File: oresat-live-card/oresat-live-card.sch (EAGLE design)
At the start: 277 parts, among them J1 ORESAT-DEBUG-CONNECTOR-CARD, J100 DM3BT-DSF-PEJS, J102 FTSH-105-XX-X-DV-K, J2 SM06B-SRSS-TB(LF)(SN), J4 TFM-120-01-L-D-RA, Q1 MMBT2907, Q2 PMV45EN, Q3 DMP2240UDM, Q4 PMV45EN, Q5 MOSFET-PCH-SOT23-6, Q6 MOSFET-PCH-SOT23-6, U1 RCLAMP0504FB, U10 TLVH431, U11 TCAN330, U12 MIC842LYC5, U13 MIC842LYC5, U14 MAX4211FETE, U15 TPS62112, U16 MAX7310ATE, U17 25AAXX, U18 RCLAMP0504FB, U2 TPS2051CDBVR, U3 THGBMJG7C2LBAU8, U4 SN74LVC1G07DCK, U7 OSD3358-512M-BSM, Y1 24MHz, Y2 ABS07-32.768KHZ-T

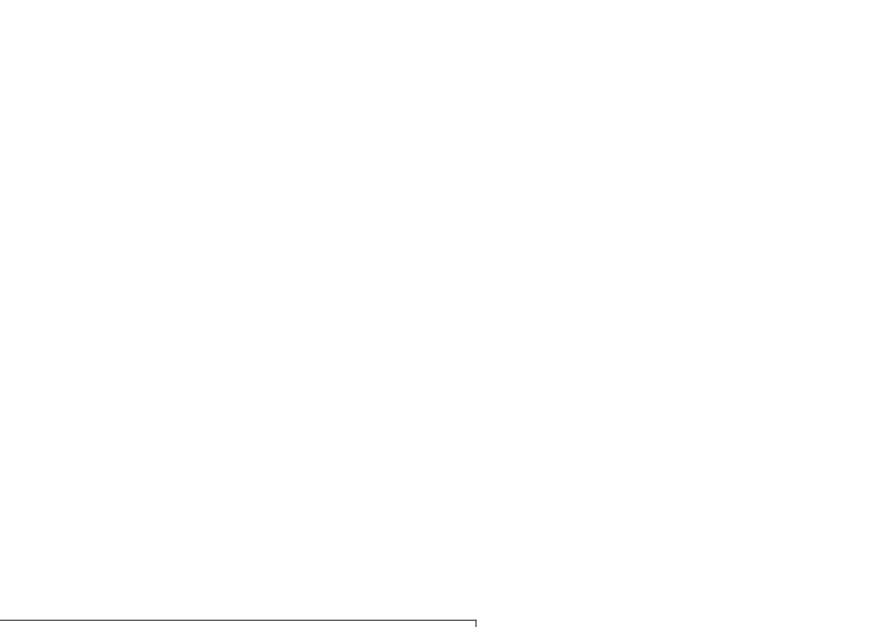
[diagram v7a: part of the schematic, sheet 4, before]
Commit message: routed usb host data for the wifi midule
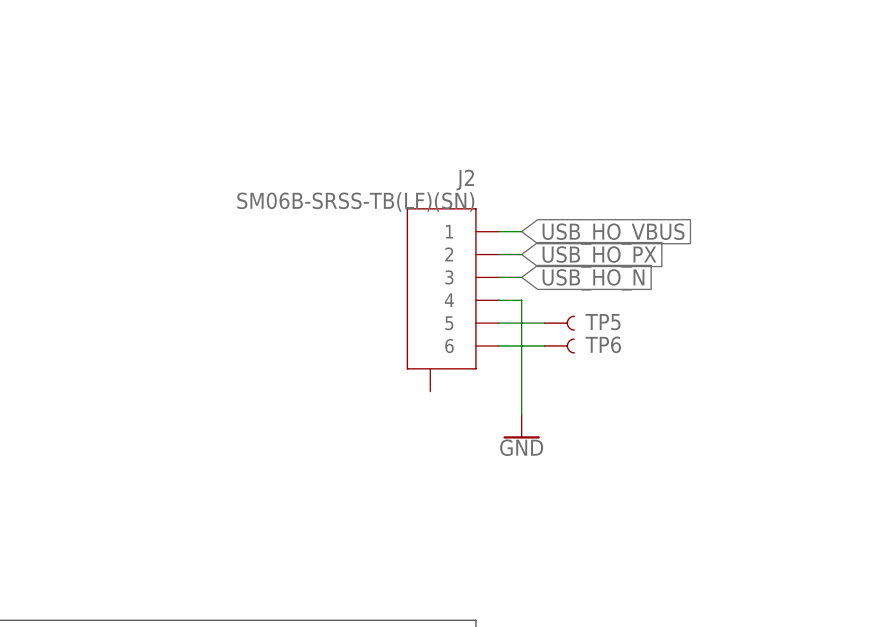
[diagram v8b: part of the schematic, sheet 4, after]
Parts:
- added TP5, TP6: TEST-POINT3X4, SparkFun-Connectors:TEST-POINT3X4
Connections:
- new net N$120: J2.5, TP5.1
- new net N$121: J2.6, TP6.1
- net GND: now also J2.4
- net USB_HO_N: now also J2.3
- net USB_HO_PX: now also J2.2
- net USB_HO_VBUS: now also J2.1
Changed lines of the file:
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@@
 <part name="PCBA1" library="PCBA-WF-NP9202-wifi-adapter" deviceset="WF-NP9202" device="WF"/>
 <part name="J2" library="J-JST-SM06B-SRSS-TB(LF)(SN)-1mm-smt-6pin" deviceset="SM06B-SRSS-TB(LF)(SN)" device=""/>
+<part name="GND33" library="SparkFun-PowerSymbols" deviceset="GND" device=""/>
+<part name="TP5" library="SparkFun-Connectors" deviceset="TEST-POINT" device="3X4" package3d_urn="urn:adsk.eagle:package:38287/1"/>
+<part name="TP6" library="SparkFun-Connectors" deviceset="TEST-POINT" device="3X4" package3d_urn="urn:adsk.eagle:package:38287/1"/>
 </parts>
 <sheets>
@@
 <attribute name="VALUE" x="223.52" y="60.96" size="1.778" layer="96"/>
 </instance>
-<instance part="J2" gate="A" x="254" y="76.2" smashed="yes" rot="MR0">
-<attribute name="NAME" x="259.08" y="86.36" size="1.778" layer="95" ratio="6" rot="SMR0"/>
-<attribute name="VALUE" x="259.08" y="83.82" size="1.778" layer="96" ratio="20" rot="MR0"/>
-</instance>
 </instances>
 <busses>
@@
 <attribute name="VALUE" x="60.96" y="190.5" size="1.778" layer="96" font="vector" align="top-left"/>
 </instance>
+<instance part="J2" gate="A" x="327.66" y="170.18" smashed="yes" rot="MR0">
+<attribute name="NAME" x="332.74" y="180.34" size="1.778" layer="95" ratio="6" rot="SMR0"/>
+<attribute name="VALUE" x="332.74" y="177.8" size="1.778" layer="96" ratio="20" rot="MR0"/>
+</instance>
+<instance part="GND33" gate="1" x="337.82" y="152.4" smashed="yes">
+<attribute name="VALUE" x="337.82" y="152.146" size="1.778" layer="96" align="top-center"/>
+</instance>
+<instance part="TP5" gate="G$1" x="340.36" y="165.1" smashed="yes">
+<attribute name="NAME" x="344.932" y="164.338" size="1.778" layer="95" font="vector"/>
+</instance>
+<instance part="TP6" gate="G$1" x="340.36" y="162.56" smashed="yes">
+<attribute name="NAME" x="344.932" y="161.798" size="1.778" layer="95" font="vector"/>
+</instance>
 </instances>
 <busses>
@@
 <wire x1="259.08" y1="137.16" x2="259.08" y2="139.7" width="0.1524" layer="91"/>
 </segment>
+<segment>
+<pinref part="J2" gate="A" pin="4"/>
+<wire x1="335.28" y1="167.64" x2="337.82" y2="167.64" width="0.1524" layer="91"/>
+<pinref part="GND33" gate="1" pin="GND"/>
+<wire x1="337.82" y1="167.64" x2="337.82" y2="154.94" width="0.1524" layer="91"/>
+</segment>
 </net>
 <net name="VIN_USB" class="0">
@@
 <label x="297.18" y="68.58" size="1.4224" layer="95" xref="yes"/>
 </segment>
+<segment>
+<pinref part="J2" gate="A" pin="1"/>
+<wire x1="335.28" y1="175.26" x2="337.82" y2="175.26" width="0.1524" layer="91"/>
+<label x="337.82" y="175.26" size="1.778" layer="95" xref="yes"/>
+</segment>
 </net>
 <net name="N$619" class="0">
@@
 <wire x1="160.02" y1="81.28" x2="160.02" y2="60.96" width="0.1524" layer="91"/>
 </segment>
+<segment>
+<pinref part="J2" gate="A" pin="3"/>
+<wire x1="335.28" y1="170.18" x2="337.82" y2="170.18" width="0.1524" layer="91"/>
+<label x="337.82" y="170.18" size="1.778" layer="95" xref="yes"/>
+</segment>
 </net>
 <net name="USB_HO_PX" class="0">
@@
 <wire x1="165.1" y1="83.82" x2="162.56" y2="83.82" width="0.1524" layer="91"/>
 </segment>
+<segment>
+<pinref part="J2" gate="A" pin="2"/>
+<wire x1="335.28" y1="172.72" x2="337.82" y2="172.72" width="0.1524" layer="91"/>
+<label x="337.82" y="172.72" size="1.778" layer="95" xref="yes"/>
+</segment>
 </net>
 <net name="N$92" class="0">
@@
 </segment>
 </net>
+<net name="N$120" class="0">
+<segment>
+<pinref part="J2" gate="A" pin="5"/>
+<pinref part="TP5" gate="G$1" pin="1"/>
+<wire x1="335.28" y1="165.1" x2="340.36" y2="165.1" width="0.1524" layer="91"/>
+</segment>
+</net>
+<net name="N$121" class="0">
+<segment>
+<pinref part="J2" gate="A" pin="6"/>
+<pinref part="TP6" gate="G$1" pin="1"/>
+<wire x1="335.28" y1="162.56" x2="340.36" y2="162.56" width="0.1524" layer="91"/>
+</segment>
+</net>
